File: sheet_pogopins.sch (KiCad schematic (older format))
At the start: 12 parts, among them P3 CONN_01X06, P4 conn_03z03, P5 CONN_02X05, U3 KNUSB

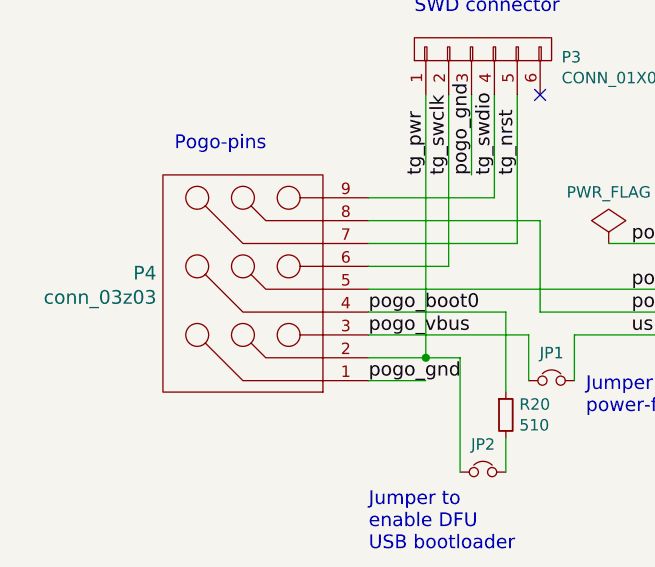
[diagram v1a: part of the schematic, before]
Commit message: Routing cleanup and silkscreen on heart.
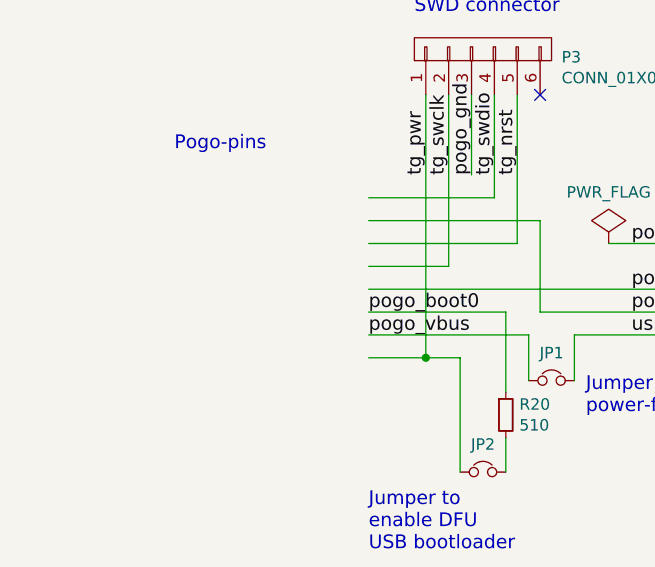
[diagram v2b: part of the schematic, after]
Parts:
- removed P4: conn_03z03, knielsenlib:pogopins_3x3_TH, symbol conn_03z03
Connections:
- wire segments 41 -> 40
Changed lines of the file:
@@
 	-1   0    0    1
 $EndComp
-$Comp
-L conn_03z03 P4
-U 1 1 576FB8FA
-P 2100 2500
-F 0 "P4" H 1622 2430 60  0000 R CNN
-F 1 "conn_03z03" H 1622 2536 60  0000 R CNN
-F 2 "knielsenlib:pogopins_3x3_TH" H 2100 2500 60  0001 C CNN
-F 3 "" H 2100 2500 60  0000 C CNN
-	1    2100 2500
-	1    0    0    1
-$EndComp
-Wire Wire Line
-	2550 2900 2800 2900
 NoConn ~ 4050 2400
 Wire Wire Line
@@
 Text Label 3700 4450 0    60   ~ 0
 pogo_gnd
-Text Label 2550 2900 0    60   ~ 0
-pogo_gnd
 Text Label 3700 2300 0    60   ~ 0

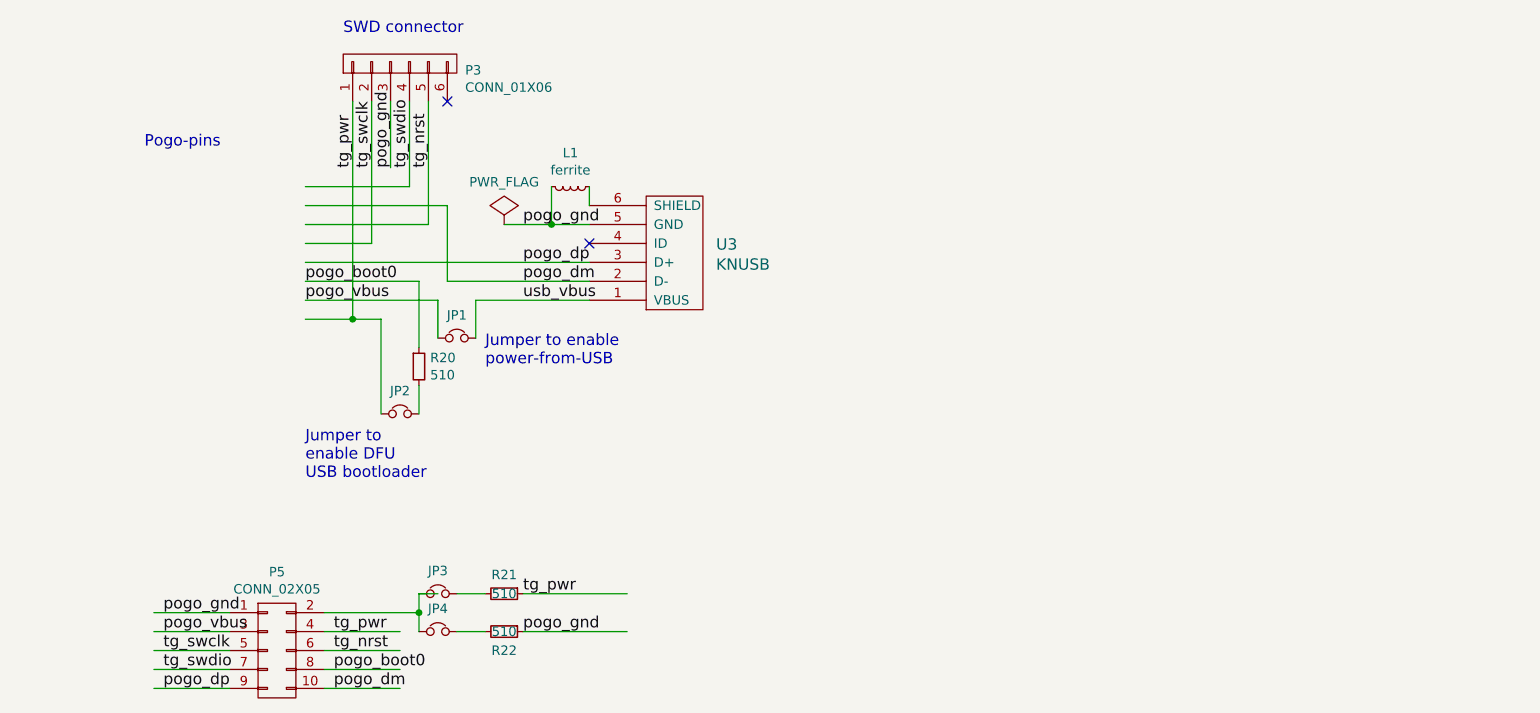
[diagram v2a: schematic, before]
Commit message: New routing of pogo-pins board (still needs some cleanup).
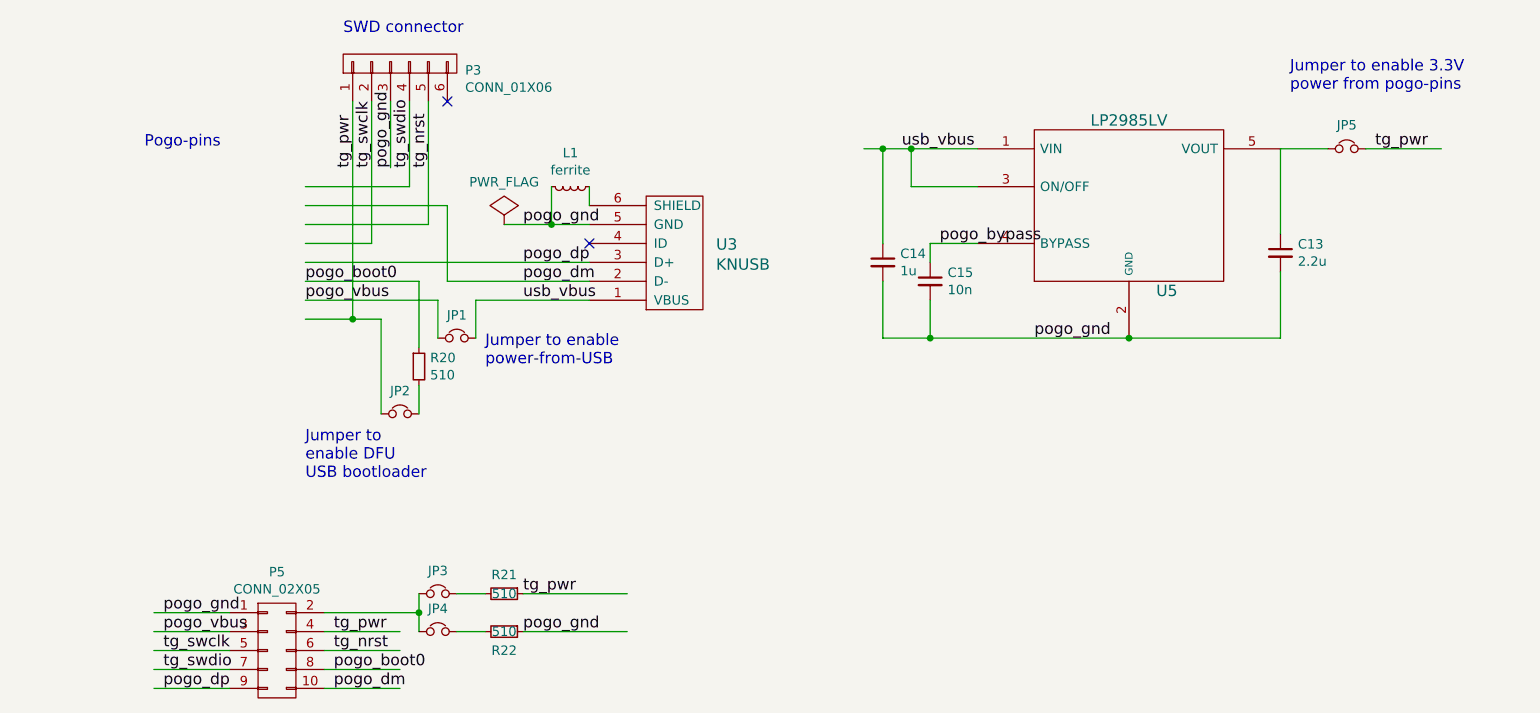
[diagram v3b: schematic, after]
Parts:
- added C13: 2.2u, Capacitors_SMD:C_0603, symbol C_Small
- added C14: 1u, Capacitors_SMD:C_0603, symbol C_Small
- added C15: 10n, Capacitors_SMD:C_0603, symbol C_Small
- added JP5: Jumper_NC_Small, Pin_Headers:Pin_Header_Straight_1x02, symbol Jumper_NC_Small
- added U5: LP2985LV, TO_SOT_Packages_SMD:SOT-23-5, symbol LP2985LV
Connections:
- net labels added: pogo_bypass
- wire segments 40 -> 52
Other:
- note added: "Jumper to enable 3.3V\npower from pogo-pins"
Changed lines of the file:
@@
 F 3 "" H 3350 2900 50  0000 C CNN
 	1    3350 2900
-	1    0    0    -1
+	-1   0    0    -1
 $EndComp
 $Comp
@@
 Wire Wire Line
 	3150 4250 3150 4450
-Wire Wire Line
-	3150 4250 3250 4250
 $Comp
 L Jumper_NC_Small JP3
@@
 F 3 "" H 3250 4250 50  0000 C CNN
 	1    3250 4250
-	1    0    0    -1
+	-1   0    0    -1
 $EndComp
 $Comp
@@
 F 3 "" H 3250 4450 50  0000 C CNN
 	1    3250 4450
-	1    0    0    -1
+	-1   0    0    -1
 $EndComp
 Connection ~ 3150 4350
@@
 	1    0    0    -1
 $EndComp
+$Comp
+L LP2985LV U5
+U 1 1 577E7501
+P 6900 2200
+F 0 "U5" H 7100 1750 60  0000 C CNN
+F 1 "LP2985LV" H 6900 2650 60  0000 C CNN
+F 2 "TO_SOT_Packages_SMD:SOT-23-5" H 6900 2200 60  0001 C CNN
+F 3 "" H 6900 2200 60  0001 C CNN
+	1    6900 2200
+	1    0    0    -1
+$EndComp
+Text Label 5900 2400 0    60   ~ 0
+pogo_bypass
+Wire Wire Line
+	5600 2600 5600 2900
+Wire Wire Line
+	5850 2700 5850 2900
+Wire Wire Line
+	7700 1900 7700 2350
+Connection ~ 5850 2900
+Connection ~ 5600 1900
+Wire Wire Line
+	5600 1900 5600 2400
+Connection ~ 5750 1900
+Wire Wire Line
+	5750 1900 5750 2100
+Wire Wire Line
+	5750 2100 6100 2100
+Connection ~ 6900 2900
+Wire Wire Line
+	7700 1900 7950 1900
+Wire Wire Line
+	5850 2400 6100 2400
+Wire Wire Line
+	5600 2900 7700 2900
+Wire Wire Line
+	5500 1900 6100 1900
+$Comp
+L C_Small C13
+U 1 1 577E7520
+P 7700 2450
+F 0 "C13" H 7792 2496 50  0000 L CNN
+F 1 "2.2u" H 7792 2405 50  0000 L CNN
+F 2 "Capacitors_SMD:C_0603" H 7700 2450 50  0001 C CNN
+F 3 "" H 7700 2450 50  0000 C CNN
+	1    7700 2450
+	1    0    0    -1
+$EndComp
+$Comp
+L C_Small C14
+U 1 1 577E7527
+P 5600 2500
+F 0 "C14" H 5692 2546 50  0000 L CNN
+F 1 "1u" H 5692 2455 50  0000 L CNN
+F 2 "Capacitors_SMD:C_0603" H 5600 2500 50  0001 C CNN
+F 3 "" H 5600 2500 50  0000 C CNN
+	1    5600 2500
+	1    0    0    -1
+$EndComp
+$Comp
+L C_Small C15
+U 1 1 577E752E
+P 5850 2600
+F 0 "C15" H 5942 2646 50  0000 L CNN
+F 1 "10n" H 5942 2555 50  0000 L CNN
+F 2 "Capacitors_SMD:C_0603" H 5850 2600 50  0001 C CNN
+F 3 "" H 5850 2600 50  0000 C CNN
+	1    5850 2600
+	1    0    0    -1
+$EndComp
+Wire Wire Line
+	5850 2400 5850 2500
+Text Label 6400 2900 0    60   ~ 0
+pogo_gnd
+Text Label 5700 1900 0    60   ~ 0
+usb_vbus
+$Comp
+L Jumper_NC_Small JP5
+U 1 1 577E763C
+P 8050 1900
+F 0 "JP5" H 8050 2025 50  0000 C CNN
+F 1 "Jumper_NC_Small" H 8060 1840 50  0001 C CNN
+F 2 "Pin_Headers:Pin_Header_Straight_1x02" H 8050 1900 50  0001 C CNN
+F 3 "" H 8050 1900 50  0000 C CNN
+	1    8050 1900
+	1    0    0    -1
+$EndComp
+Wire Wire Line
+	8150 1900 8550 1900
+Text Label 8200 1900 0    60   ~ 0
+tg_pwr
+Wire Wire Line
+	7700 2900 7700 2550
+Text Notes 7750 1600 0    60   ~ 0
+Jumper to enable 3.3V\npower from pogo-pins
 $EndSCHEMATC
